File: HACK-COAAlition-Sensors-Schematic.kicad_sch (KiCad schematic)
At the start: 5 parts, among them U1 Pico, U2 XC7V585T-FFG1157, U4 DHT11

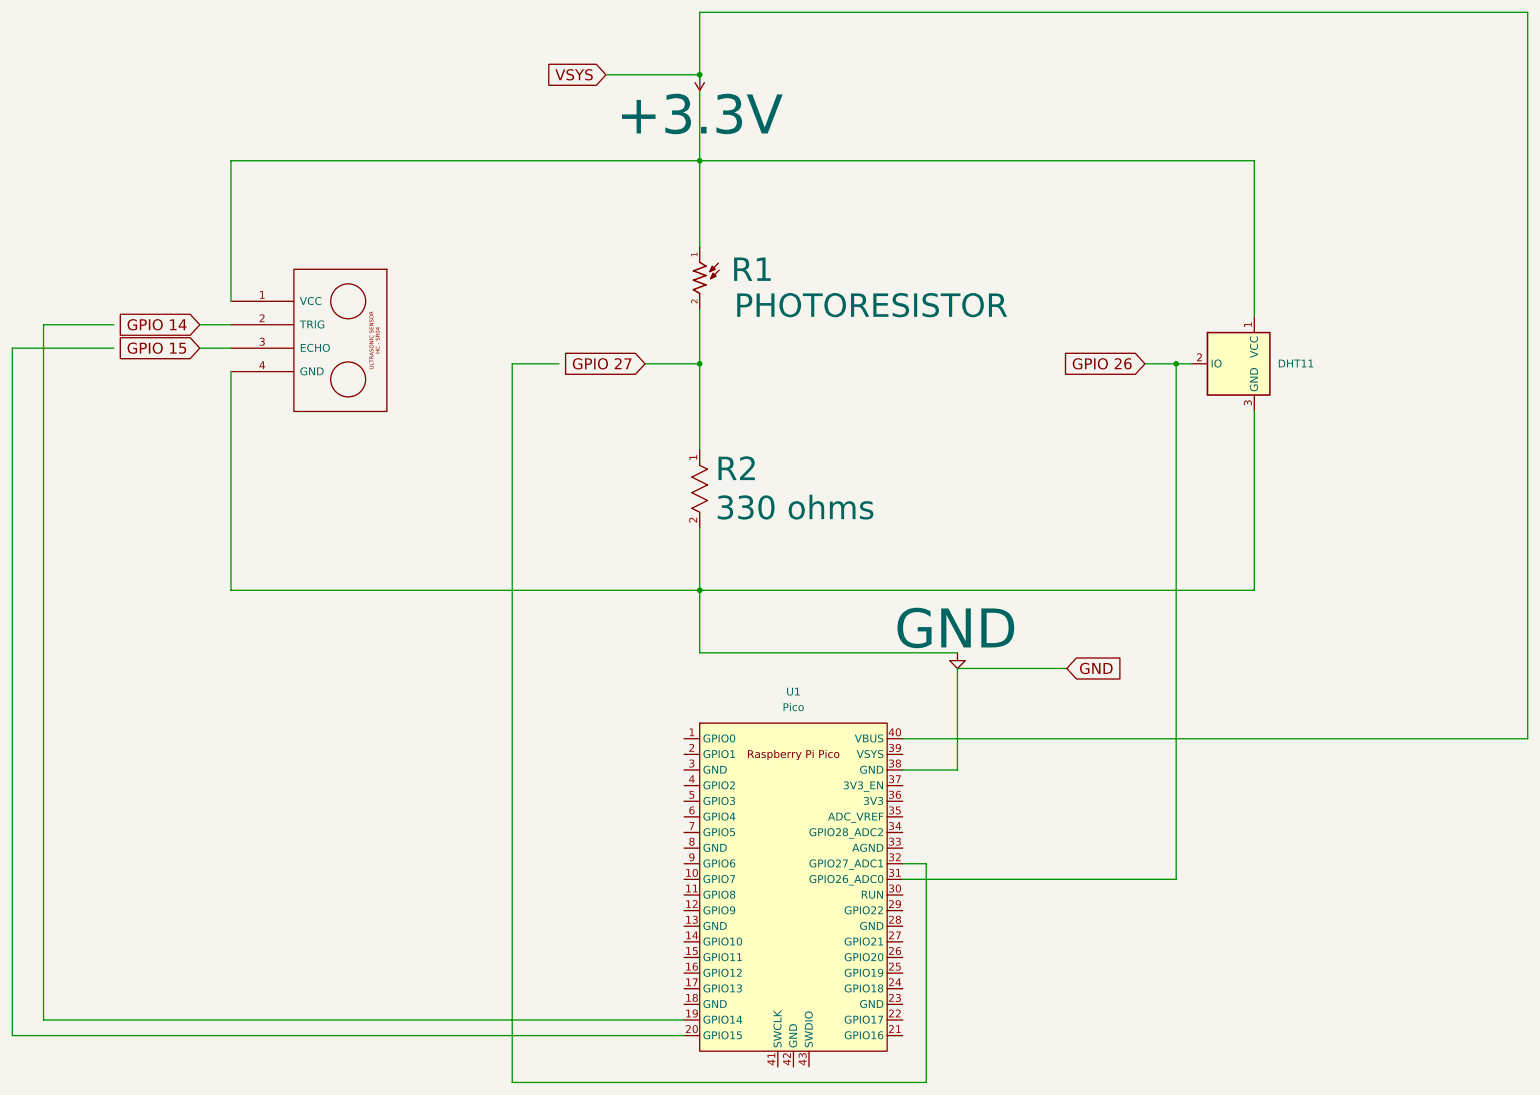
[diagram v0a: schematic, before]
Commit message: updated Pager CAD file
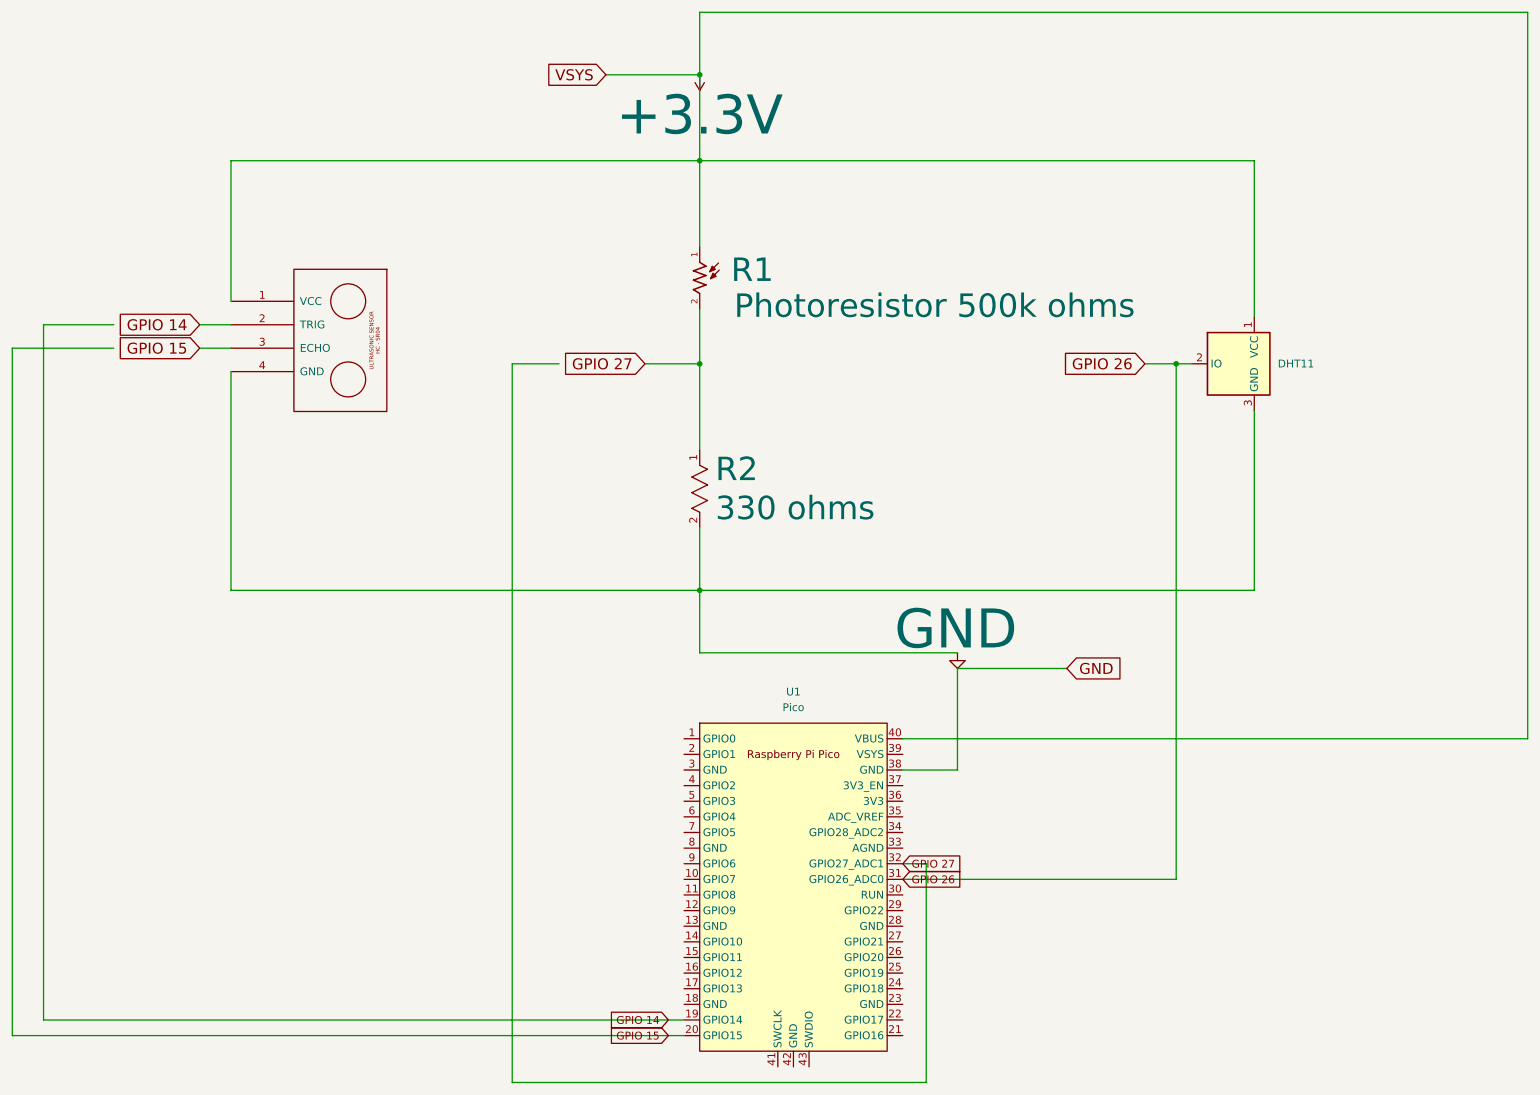
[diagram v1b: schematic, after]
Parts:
- R1: value PHOTORESISTOR -> Photoresistor 500k ohms
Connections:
- net GPIO 14: now also U1.19 (GPIO14)
- net GPIO 15: now also U1.20 (GPIO15)
- net GPIO 27: now also U1.32 (GPIO27_ADC1)
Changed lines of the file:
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@@
+		)
+	)
+	(global_label "GPIO 14"
+		(shape input)
+		(at 130.81 186.69 180)
+		(fields_autoplaced yes)
+		(effects
+			(font
+				(size 1.27 1.27)
+			)
+			(justify right)
+		)
+		(property "Intersheetrefs" "${INTERSHEET_REFS}"
+			(at 119.9629 186.69 0)
+			(effects
+				(font
+					(size 1.27 1.27)
+				)
+				(justify right)
+				(hide yes)
+			)
 		)
 	)
@@
 		)
 	)
+	(global_label "GPIO 26"
+		(shape input)
+		(at 168.91 163.83 0)
+		(fields_autoplaced yes)
+		(effects
+			(font
+				(size 1.27 1.27)
+			)
+			(justify left)
+		)
+		(property "Intersheetrefs" "${INTERSHEET_REFS}"
+			(at 179.7571 163.83 0)
+			(effects
+				(font
+					(size 1.27 1.27)
+				)
+				(justify left)
+				(hide yes)
+			)
+		)
+	)
 	(global_label "GND"
 		(shape input)
@@
 		(property "Intersheetrefs" "${INTERSHEET_REFS}"
 			(at 110.0364 33.02 0)
+			(effects
+				(font
+					(size 1.27 1.27)
+				)
+				(justify right)
+				(hide yes)
+			)
+		)
+	)
+	(global_label "GPIO 27"
+		(shape input)
+		(at 168.91 161.29 0)
+		(fields_autoplaced yes)
+		(effects
+			(font
+				(size 1.27 1.27)
+			)
+			(justify left)
+		)
+		(property "Intersheetrefs" "${INTERSHEET_REFS}"
+			(at 179.7571 161.29 0)
+			(effects
+				(font
+					(size 1.27 1.27)
+				)
+				(justify left)
+				(hide yes)
+			)
+		)
+	)
+	(global_label "GPIO 15"
+		(shape input)
+		(at 130.81 189.23 180)
+		(fields_autoplaced yes)
+		(effects
+			(font
+				(size 1.27 1.27)
+			)
+			(justify right)
+		)
+		(property "Intersheetrefs" "${INTERSHEET_REFS}"
+			(at 119.9629 189.23 0)
 			(effects
 				(font
@@
 			)
 		)
-		(property "Value" "PHOTORESISTOR"
+		(property "Value" "Photoresistor 500k ohms"
 			(at 141.478 70.612 90)
 			(effects
